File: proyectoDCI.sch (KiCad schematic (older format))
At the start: 0 parts

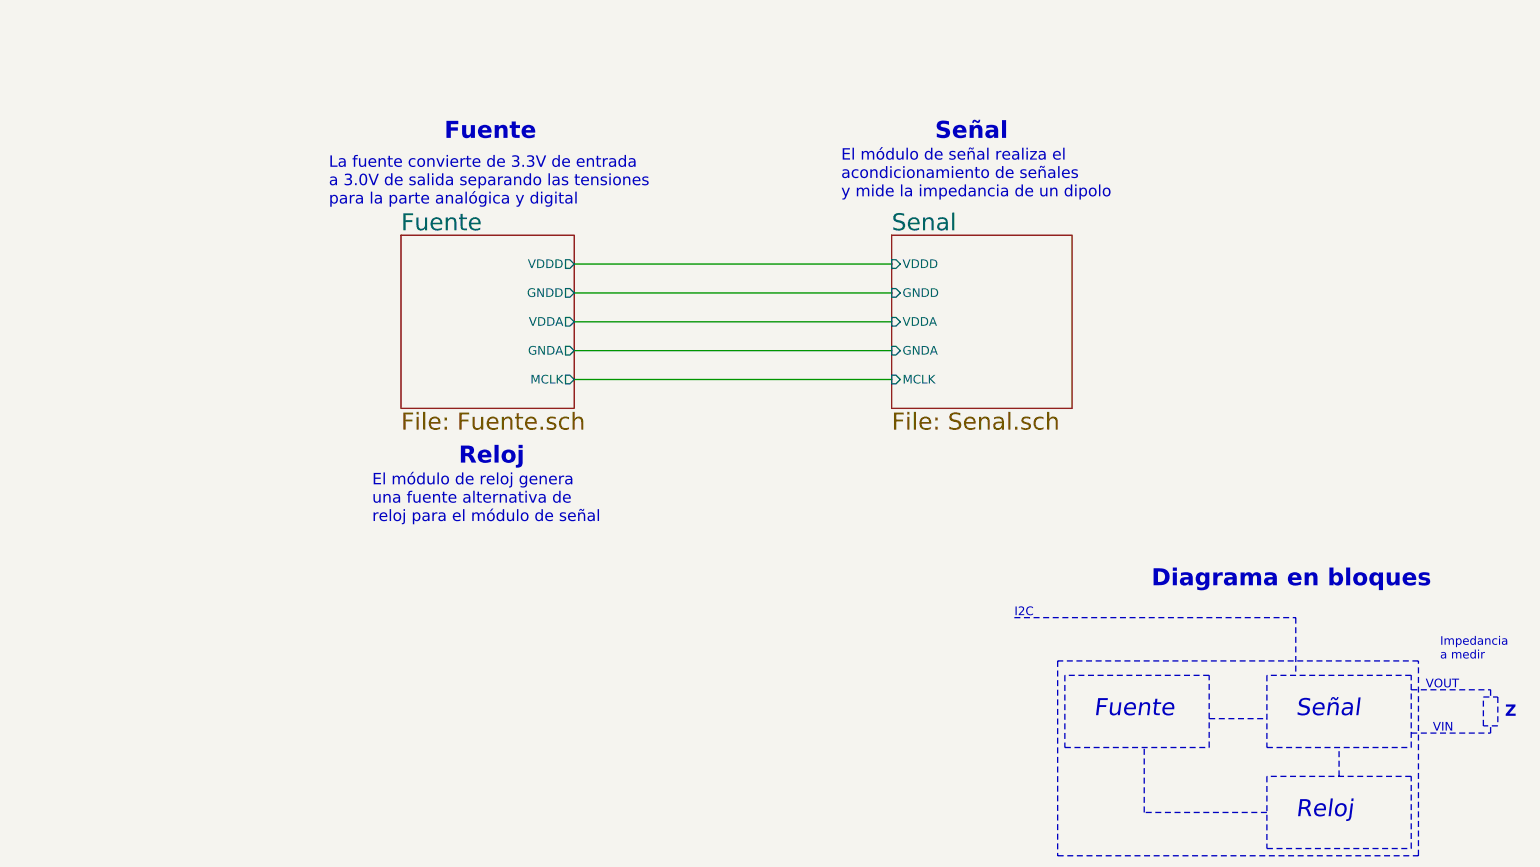
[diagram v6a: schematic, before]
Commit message: Se agregaron los campos Digikey#
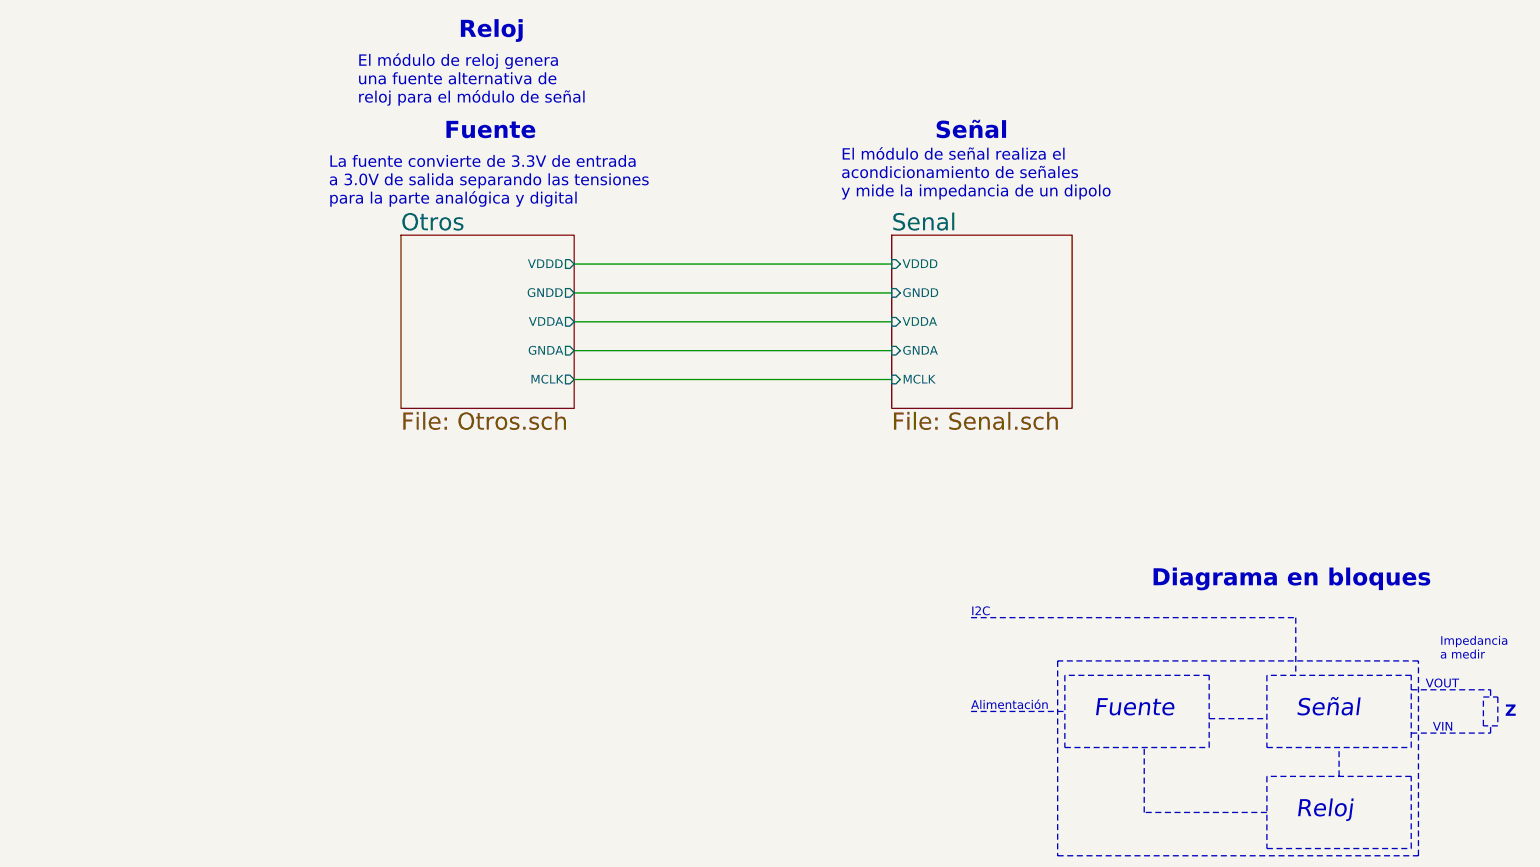
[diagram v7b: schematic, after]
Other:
- note added: "Alimentación"
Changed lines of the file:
@@
 Impedancia\na medir
 Wire Notes Line
-	7500 4750 9450 4750
+	7200 4750 9450 4750
 Wire Notes Line
 	9450 4750 9450 5150
-Text Notes 7500 4750 0    60   ~ 0
+Text Notes 7200 4750 0    60   ~ 0
 I2C
 $Sheet
@@
 Text Notes 6300 1850 0    79   ~ 0
 El módulo de señal realiza el \nacondicionamiento de señales \ny mide la impedancia de un dipolo
-Text Notes 3650 3700 0    118  ~ 24
+Text Notes 3650 750  0    118  ~ 24
 Reloj
-Text Notes 3050 4100 0    79   ~ 0
+Text Notes 2950 1200 0    79   ~ 0
 El módulo de reloj genera\nuna fuente alternativa de \nreloj para el módulo de señal
 Wire Notes Line
@@
 S 3250 2100 1200 1200
 U 582DA8A0
-F0 "Fuente" 118
-F1 "Fuente.sch" 118
+F0 "Otros" 118
+F1 "Otros.sch" 118
 F2 "VDDD" O R 4450 2300 60
 F3 "GNDD" O R 4450 2500 60
@@
 Wire Wire Line
 	4450 3100 6650 3100
+Wire Notes Line
+	7200 5400 7850 5400
+Text Notes 7200 5400 0    60   ~ 0
+Alimentación
 $EndSCHEMATC
